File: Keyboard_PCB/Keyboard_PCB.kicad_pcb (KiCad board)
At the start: 4 copper layers, 107 parts, among them J1 I2C_LCD, J2 USB-C 16P, J3 LCD_MODULE, J4 FPC 30, J5 JTAG, Q1 S8050, SW1 EC11E15244G1, SW2 BTN, SW3 BTN, SW4 BTN, U1 STM32F412CGUx, U2 USBLC6-2SC6, U5 MCP73871, U6 MCP73871, U7 W25Q128JVS, Y1 25MHz, Y2 32.768 KHz

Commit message: Battery charger layout done
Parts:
- removed C24: 22u, Capacitor_SMD:C_0603_1608Metric
- removed C25: 100n, Capacitor_SMD:C_0603_1608Metric
- removed C26, C27, C33, C34: 4u7, Capacitor_SMD:C_0603_1608Metric
- removed C31, C32: 10u, Capacitor_SMD:C_0603_1608Metric
- removed JP2: BAT_BYP, Jumper:SolderJumper-2_P1.3mm_Open_TrianglePad1.0x1.5mm
- removed R16, R17, R18, R19: 470, Resistor_SMD:R_0603_1608Metric
- removed R20, R21: 10k, Resistor_SMD:R_0603_1608Metric
- removed TP1, TP2: TestPoint, TestPoint:TestPoint_Pad_D1.0mm
- added D11: PG, LED_SMD:LED_0603_1608Metric, F.Cu at (100.0, 206.6)
- added D4: BAT54C, Package_TO_SOT_SMD:SOT-23, F.Cu at (116.8, 197.0)
- C15: value 10u -> 22u
- C17: value 22u -> 10u
- C19: value 100n -> 22u
- C20, C21: value 10u -> 1u
- C22, C23: value 22u -> 1u
- D5: value PG -> BAT54C; footprint LED_SMD:LED_0603_1608Metric -> Package_TO_SOT_SMD:SOT-23
- L2, L3: value 1u5 -> 1u
- Q1: footprint Package_TO_SOT_THT:TO-92_Inline -> Package_TO_SOT_SMD:SOT-23
- R10, R13: value 180k -> 470
- R11, R9: value 1M -> 470
- R12, R8: value 1M -> 10k
- TH1, TH2: value Thermistor_NTC -> 10k
- U2: value USBLC6-2SC6 -> ISL91127IR; footprint Package_TO_SOT_SMD:SOT-23-6 -> Package_DFN_QFN:QFN-20-1EP_4x4mm_P0.5mm_EP2.7x2.7mm_ThermalVias
- U3: value ~ -> USBLC6-2SC6; footprint Marijn_KiCad:QFN_DSJ -> Package_TO_SOT_SMD:SOT-23-6
- U4: value ~ -> ISL91127IR; footprint Marijn_KiCad:QFN_DSJ -> Package_DFN_QFN:QFN-20-1EP_4x4mm_P0.5mm_EP2.7x2.7mm_ThermalVias
- U5, U6: value MCP73871 -> MCP73833; footprint Package_DFN_QFN:QFN-20-1EP_4x4mm_P0.5mm_EP2.5x2.5mm -> Package_DFN_QFN:DFN-10-1EP_3x3mm_P0.5mm_EP1.58x2.35mm
- moved U3 149.2 mm to (245.7, 156.6), turned to 0 degrees
- moved FL1 134.9 mm to (230.5, 168.4)
- moved Q1 65.7 mm to (273.9, 139.4)
- moved BT2 60.5 mm to (113.0, 202.2)
- moved U2 57.4 mm to (132.1, 195.1), turned to 0 degrees
- moved L3 56.7 mm to (137.5, 196.1)
- moved U6 56.7 mm to (107.4, 204.0), turned to 0 degrees
- moved D8 55.6 mm to (100.0, 199.9), turned to 180 degrees
- moved D10 55.6 mm to (100.0, 205.1), turned to 180 degrees
- moved D9 54.5 mm to (100.0, 203.5), turned to 180 degrees
- moved C20 51.0 mm to (105.9, 194.7), turned to 0 degrees
- moved C21 50.9 mm to (109.0, 194.7), turned to 180 degrees
- moved R11 47.8 mm to (103.1, 199.9), turned to 180 degrees
- moved TH2 46.7 mm to (110.4, 205.1), turned to -90 degrees
- moved U4 46.1 mm to (132.1, 201.3), turned to 0 degrees
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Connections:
- BT1 pad 1: Net-(BT1-+) -> /USB_PWR/APP_BAT
- BT2 pad 1: Net-(BT2-+) -> /USB_PWR/BKUP_BAT
- C14 pad 1: V_IN -> PVIN
- C15 pad 1: V_IN -> +3V3
- C17 pad 1: +3V3 -> PVIN
- C18 pad 1: +3V3 -> /VBAT
- C19 pad 1: Net-(U3-EN) -> /VBAT
- C20 pad 1: VIN -> +5V
- C21 pad 1: VIN -> /USB_PWR/APP_BAT
- C22 pad 1: /VBAT -> +5V
- C23 pad 1: /VBAT -> /USB_PWR/BKUP_BAT
- D5 pad 1: Net-(D5-K) -> /USB_PWR/BKUP_BAT
- Q1 pad 1: GND -> Net-(Q1-B)
- Q1 pad 2: Net-(Q1-B) -> GND
- R10 pad 1: Net-(U3-FB) -> Net-(U5-STAT2)
- R10 pad 2: GND -> Net-(D7-K)
- R11 pad 1: /VBAT -> Net-(U5-~{PG})
- R11 pad 2: Net-(U4-FB) -> Net-(D8-K)
- R12 pad 1: /VBAT -> GND
- R12 pad 2: /USB_PWR/PG1 -> /USB_PWR/BKUP_PROG
- R13 pad 1: Net-(U4-FB) -> Net-(U6-STAT1)
- R13 pad 2: GND -> Net-(D9-K)
- R14 pad 1: Net-(D5-K) -> Net-(U6-STAT2)
- R14 pad 2: /USB_PWR/APP_PG -> Net-(D10-K)
- R15 pad 1: Net-(D6-K) -> Net-(U6-~{PG})
- R15 pad 2: /USB_PWR/APP_STAT1 -> Net-(D11-K)
- R8 pad 1: +3V3 -> GND
- R8 pad 2: Net-(U3-FB) -> /USB_PWR/APP_PROG
- R9 pad 1: +3V3 -> Net-(U5-STAT1)
- R9 pad 2: /USB_PWR/PG0 -> Net-(D6-K)
- U1 pad 18: /APP_FC -> unconnected-(U1-PB0-Pad18)
- U1 pad 19: /BKUP_FC -> unconnected-(U1-PB1-Pad19)
- U2 pad 1: Net-(J2-D--PadA7) -> Net-(L2-Pad2)
- U2 pad 2: GND -> Net-(L2-Pad2)
- U2 pad 3: Net-(J2-D+-PadA6) -> GND
- U2 pad 4: Net-(FL1-Pad4) -> Net-(L2-Pad1)
- U2 pad 5: +5V -> Net-(L2-Pad1)
- U2 pad 6: Net-(FL1-Pad1) -> PVIN
- U3 pad 1: Net-(U3-EN) -> Net-(J2-D--PadA7)
- U3 pad 3: Net-(U3-FB) -> Net-(J2-D+-PadA6)
- U3 pad 4: +3V3 -> Net-(FL1-Pad4)
- U3 pad 5: +3V3 -> +5V
- U3 pad 6: Net-(L2-Pad2) -> Net-(FL1-Pad1)
- U4 pad 1: Net-(U4-EN) -> Net-(L3-Pad2)
- U4 pad 10: VIN -> PVIN
- U4 pad 11: VIN -> PVIN
- U4 pad 12: Net-(U4-EN) -> PVIN
- U4 pad 13: Net-(U4-EN) -> GND
- U4 pad 14: /USB_PWR/PG1 -> GND
- U4 pad 15: GND -> /VBAT
- U4 pad 2: GND -> Net-(L3-Pad2)
- U4 pad 3: Net-(U4-FB) -> GND
- U4 pad 4: /VBAT -> Net-(L3-Pad1)
- U4 pad 5: /VBAT -> Net-(L3-Pad1)
- U4 pad 6: Net-(L3-Pad2) -> PVIN
- U4 pad 7: Net-(L3-Pad2) -> PVIN
- U4 pad 8: Net-(L3-Pad1) -> PVIN
- U4 pad 9: Net-(L3-Pad1) -> PVIN
- U5 pad 1: V_IN -> +5V
- U5 pad 10: GND -> /USB_PWR/APP_BAT
- U5 pad 3: GND -> Net-(U5-STAT1)
- U5 pad 4: /APP_FC -> Net-(U5-STAT2)
- U5 pad 5: /USB_PWR/APP_THERM -> GND
- U5 pad 6: /USB_PWR/APP_PG -> /USB_PWR/APP_PROG
- U5 pad 7: /USB_PWR/APP_STAT2 -> Net-(U5-~{PG})
- U5 pad 8: /USB_PWR/APP_STAT1 -> /USB_PWR/APP_THERM
- U5 pad 9: +5V -> /USB_PWR/APP_BAT
- U6 pad 1: VIN -> +5V
- U6 pad 10: GND -> /USB_PWR/BKUP_BAT
- U6 pad 3: GND -> Net-(U6-STAT1)
- U6 pad 4: /BKUP_FC -> Net-(U6-STAT2)
- U6 pad 5: /USB_PWR/BKUP_THERM -> GND
- U6 pad 6: /USB_PWR/BKUP_PG -> /USB_PWR/BKUP_PROG
- U6 pad 7: /USB_PWR/BKUP_STAT2 -> Net-(U6-~{PG})
- U6 pad 8: /USB_PWR/BKUP_STAT1 -> /USB_PWR/BKUP_THERM
- U6 pad 9: +5V -> /USB_PWR/BKUP_BAT
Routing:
- net +5V: track 10.9 -> 27.3 mm, vias 4 -> 0
- net /USB_PWR/APP_STAT2: track 13.6 -> 0.00 mm, vias 2 -> 0
- net /USB_PWR/APP_PG: track 13.4 -> 0.00 mm, vias 2 -> 0
- net /USB_PWR/PG0: track 12.8 -> 0.00 mm, vias 2 -> 0
- net /USB_PWR/PG1: track 12.8 -> 0.00 mm, vias 2 -> 0
- net /USB_PWR/APP_STAT1: track 10.4 -> 0.00 mm, vias 2 -> 0
- net GND: track 13.7 -> 4.31 mm, vias 73 -> 0
- net Net-(U5-~{PG}): track 0.00 -> 8.08 mm, vias 0 -> 2
- net Net-(U6-~{PG}): track 0.00 -> 8.07 mm, vias 0 -> 2
- net Net-(U4-EN): track 7.45 -> 0.00 mm, vias 2 -> 0
- net Net-(U3-EN): track 7.45 -> 0.00 mm, vias 2 -> 0
- net Net-(U4-FB): track 3.13 -> 0.00 mm
- net Net-(U3-FB): track 3.13 -> 0.00 mm
- net Net-(U6-STAT2): track 0.00 -> 2.32 mm
- net Net-(U5-STAT2): track 0.00 -> 2.32 mm
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- added copper zone on F.Cu, net /USB_PWR/APP_BAT
- added copper zone on F.Cu, net /USB_PWR/APP_PROG
- added copper zone on F.Cu, net /USB_PWR/BKUP_BAT
- added copper zone on F.Cu, net /USB_PWR/BKUP_PROG
- removed copper zone on F.Cu, net +3V3
- removed copper zone on F.Cu, net +5V
- removed copper zone on F.Cu, net /VBAT
- removed copper zone on F.Cu, net GND
- removed copper zone on F.Cu, net Net-(BT1-+)
- removed copper zone on F.Cu, net Net-(L2-Pad1)
- removed copper zone on F.Cu, net Net-(L2-Pad2)
- removed copper zone on F.Cu, net Net-(L3-Pad1)
- removed copper zone on F.Cu, net Net-(L3-Pad2)
- removed copper zone on F.Cu, net VIN
- removed copper zone on F.Cu, net V_IN

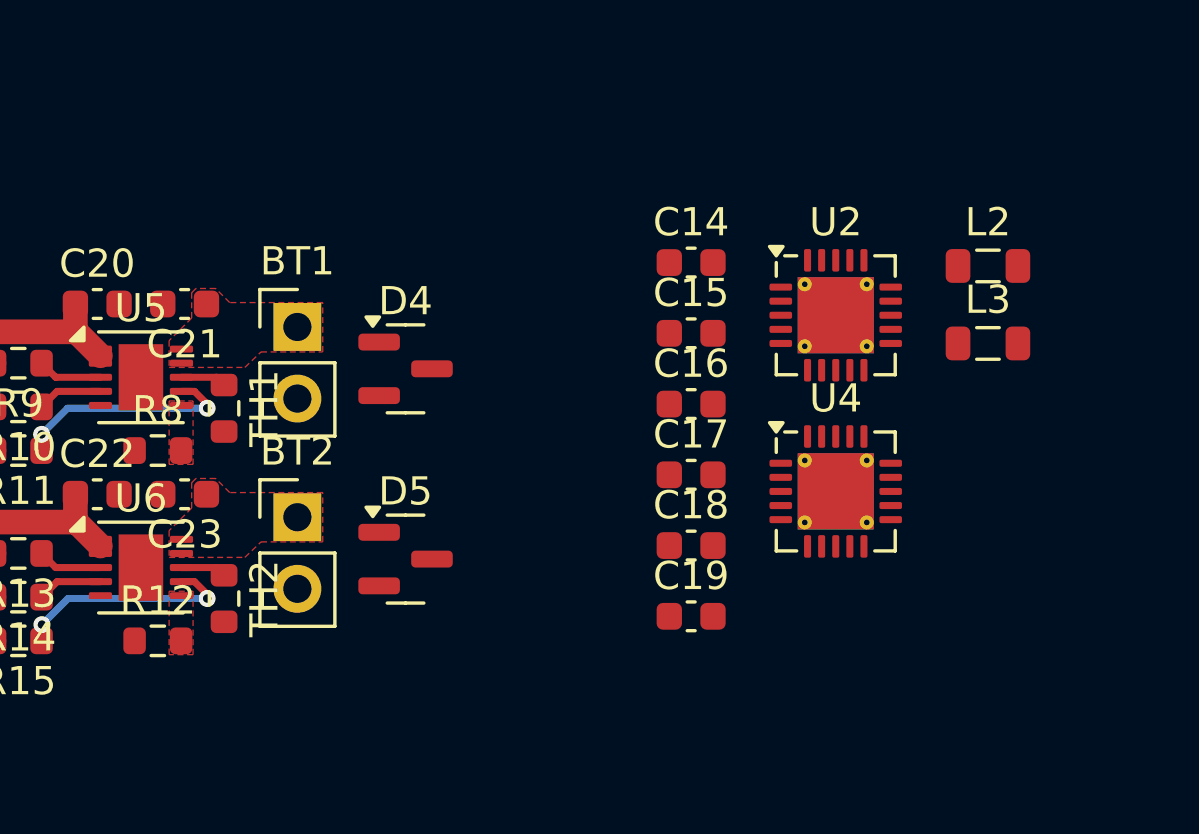
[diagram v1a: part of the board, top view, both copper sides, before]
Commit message: Buck layout progress
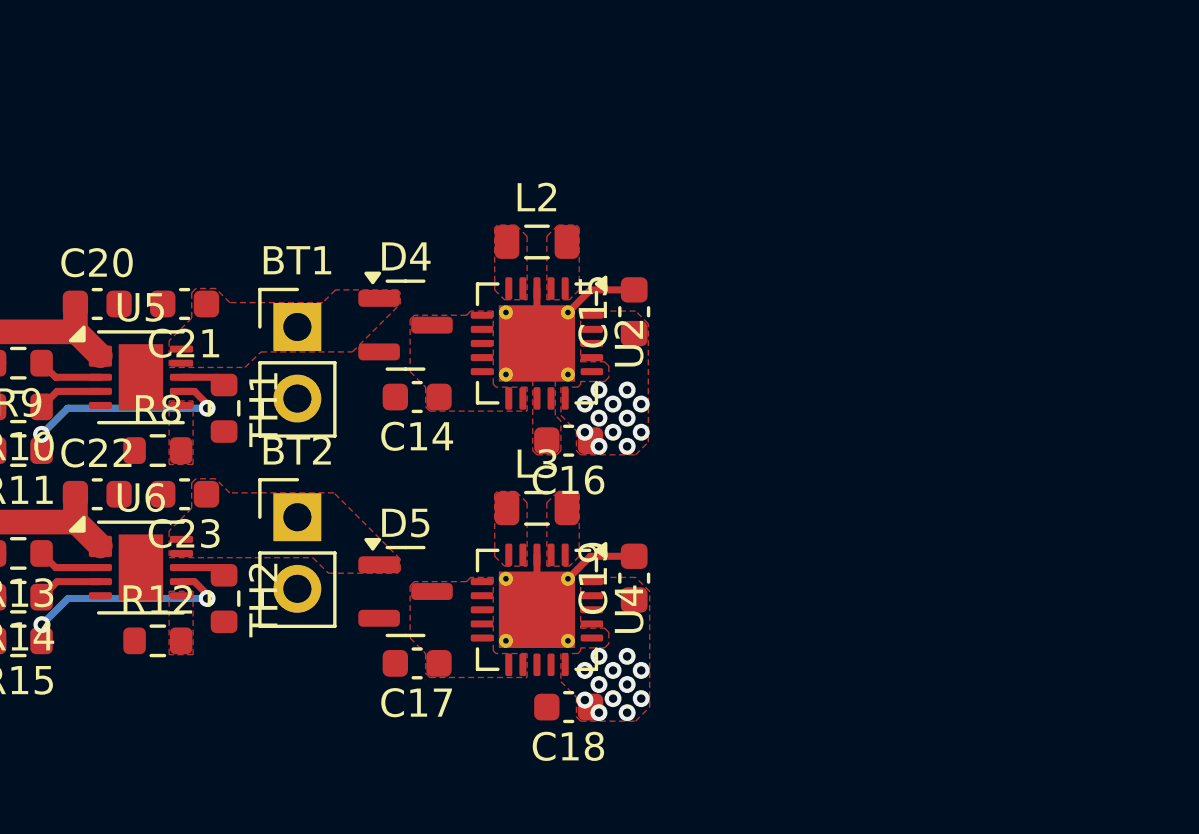
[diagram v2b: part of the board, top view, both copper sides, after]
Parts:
- moved L3 17.0 mm to (121.5, 201.9)
- moved L2 16.0 mm to (121.5, 192.5)
- moved C17 11.8 mm to (117.2, 207.4), turned to 180 degrees
- moved U4 11.4 mm to (121.5, 205.5), turned to -90 degrees
- moved C14 10.8 mm to (117.2, 198.0), turned to 180 degrees
- moved U2 10.6 mm to (121.5, 196.1), turned to -90 degrees
- moved C18 7.19 mm to (122.6, 209.0), turned to 180 degrees
- moved C16 4.54 mm to (122.6, 199.5), turned to 180 degrees
- moved C19 2.43 mm to (124.9, 204.4), turned to 90 degrees
- moved C15 2.16 mm to (124.9, 194.9), turned to 90 degrees
- moved D4 1.55 mm to (116.8, 195.4)
- moved D5 1.15 mm to (116.8, 204.9)
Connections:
- C14 pad 1: PVIN -> /USB_PWR/PVIN_APP
- C17 pad 1: PVIN -> /USB_PWR/PVIN_BKUP
- D4 pad 3: PVIN -> /USB_PWR/PVIN_APP
- D5 pad 3: PVIN -> /USB_PWR/PVIN_BKUP
- U2 pad 10: PVIN -> /USB_PWR/PVIN_APP
- U2 pad 11: PVIN -> /USB_PWR/PVIN_APP
- U2 pad 12: PVIN -> /USB_PWR/PVIN_APP
- U2 pad 6: PVIN -> /USB_PWR/PVIN_APP
- U2 pad 7: PVIN -> /USB_PWR/PVIN_APP
- U2 pad 8: PVIN -> /USB_PWR/PVIN_APP
- U2 pad 9: PVIN -> /USB_PWR/PVIN_APP
- U4 pad 10: PVIN -> /USB_PWR/PVIN_BKUP
- U4 pad 11: PVIN -> /USB_PWR/PVIN_BKUP
- U4 pad 12: PVIN -> /USB_PWR/PVIN_BKUP
- U4 pad 6: PVIN -> /USB_PWR/PVIN_BKUP
- U4 pad 7: PVIN -> /USB_PWR/PVIN_BKUP
- U4 pad 8: PVIN -> /USB_PWR/PVIN_BKUP
- U4 pad 9: PVIN -> /USB_PWR/PVIN_BKUP
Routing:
- net GND: track 4.31 -> 15.1 mm
- net /VBAT: vias 0 -> 12
- net +3V3: vias 0 -> 12
- added copper zone on F.Cu, net +3V3
- added copper zone on F.Cu, net /USB_PWR/PVIN_APP
- added copper zone on F.Cu, net /USB_PWR/PVIN_BKUP
- added copper zone on F.Cu, net /VBAT
- added copper zone on F.Cu, net GND
- added copper zone on F.Cu, net Net-(L2-Pad1)
- added copper zone on F.Cu, net Net-(L2-Pad2)
- added copper zone on F.Cu, net Net-(L3-Pad1)
- added copper zone on F.Cu, net Net-(L3-Pad2)

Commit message: Buck layout finished
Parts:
- added H1: MountingHole_Pad, MountingHole:MountingHole_2.2mm_M2_Pad_Via, F.Cu at (88.0, 192.1)
- added H2: MountingHole_Pad, MountingHole:MountingHole_2.2mm_M2_Pad_Via, F.Cu at (129.0, 192.1)
- U3: moved to B.Cu
- moved Q1 198.0 mm to (104.0, 241.0)
- moved U3 163.5 mm to (88.2, 200.6), turned to 180 degrees
- moved C10 138.7 mm to (84.7, 232.8)
- moved C11 138.7 mm to (84.7, 235.3)
- moved C12 138.7 mm to (84.7, 237.9)
- moved C13 138.7 mm to (84.7, 240.4)
- moved C28 138.7 mm to (84.7, 242.9)
- moved C29 138.7 mm to (84.7, 245.4)
- moved C30 138.7 mm to (84.7, 247.9)
- moved C35 138.7 mm to (84.7, 250.4)
- moved C4 138.7 mm to (80.7, 240.4)
- moved C7 138.7 mm to (80.7, 247.9)
- moved J1 138.7 mm to (108.4, 253.5)
- moved J3 138.7 mm to (97.0, 233.9)
- moved JP1 138.7 mm to (101.5, 267.2)
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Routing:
- net Net-(FL1-Pad4): track 0.00 -> 14.1 mm, vias 0 -> 1
- net +5V: track 27.3 -> 40.9 mm, vias 0 -> 11
- net Net-(FL1-Pad1): track 0.00 -> 9.50 mm, vias 0 -> 1
- net GND: track 15.1 -> 23.2 mm, vias 0 -> 46
- net Net-(J2-D--PadA7): track 3.92 -> 5.65 mm
- net Net-(J2-D+-PadA6): track 3.92 -> 5.65 mm
- net Net-(F1-Pad1): track 9.51 -> 8.02 mm
- net /USB_SENS: track 8.60 -> 9.94 mm
- added copper zone on B.Cu, net +5V
- added copper zone on F.Cu, net +5V
- added copper zone on B.Cu, net GND
- added copper zone on In1.Cu, net GND
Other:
- board outline added: 47 x 21.5 mm

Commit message: Power section finished
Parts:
- added JP2: WKUP_EXTI, Jumper:SolderJumper-2_P1.3mm_Open_TrianglePad1.0x1.5mm, F.Cu at (126.1, 239.9)
- added TP1: 5V, TestPoint:TestPoint_Pad_D2.0mm, F.Cu at (97.0, 198.3)
- added TP2: 3V3, TestPoint:TestPoint_Pad_D1.5mm, F.Cu at (125.3, 201.0)
- added TP3: Vbat, TestPoint:TestPoint_Pad_D1.5mm, F.Cu at (125.3, 206.6)
- J3: footprint Connector_PinHeader_2.54mm:PinHeader_1x08_P2.54mm_Vertical -> Connector_PinHeader_2.54mm:PinHeader_2x04_P2.54mm_Vertical
- SW2: footprint Button_Switch_SMD:SW_SPST_PTS810 -> Button_Switch_Keyboard:SW_Cherry_MX_1.00u_PCB
- moved H2 44.4 mm to (88.0, 209.1)
- moved SW2 39.5 mm to (142.0, 248.9)
- moved J3 17.9 mm to (95.3, 251.7)
- moved FL1 11.4 mm to (92.2, 207.8), turned to 0 degrees
- moved SW1 10.8 mm to (121.3, 263.8), turned to 90 degrees
- moved U1 1.47 mm to (112.9, 238.9)
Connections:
- U1 pad 18: unconnected-(U1-PB0-Pad18) -> Net-(JP2-B)
- U1 pad 19: unconnected-(U1-PB1-Pad19) -> /ENC_SW
- U1 pad 20: /ENC_SW -> unconnected-(U1-PB2-Pad20)
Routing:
- net Net-(FL1-Pad4): track 14.1 -> 9.13 mm
- net +3V3: track 0.00 -> 3.03 mm
- net Net-(FL1-Pad1): track 9.50 -> 11.8 mm
- net GND: vias 46 -> 90
- net /VBAT: vias 12 -> 0
- added copper zone on In2.Cu, net +3V3
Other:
- board size 47 x 21.5 mm -> 41.8 x 21.5 mm

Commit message: Layout V1
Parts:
- added H3: MountingHole_Pad, MountingHole:MountingHole_2.2mm_M2_Pad_Via, F.Cu at (88.0, 248.6)
- added H4: MountingHole_Pad, MountingHole:MountingHole_2.2mm_M2_Pad_Via, F.Cu at (124.0, 248.6)
- C11, C12, Q1, R26, R27, R28: moved to B.Cu
- moved JP1 60.7 mm to (124.8, 211.2)
- moved D2 58.7 mm to (125.6, 217.1), turned to 90 degrees
- moved D1 55.7 mm to (124.0, 217.1), turned to 90 degrees
- moved SW4 54.6 mm to (119.3, 211.1)
- moved R25 53.6 mm to (125.6, 214.0), turned to -90 degrees
- moved R24 50.7 mm to (124.0, 214.0), turned to -90 degrees
- moved L1 50.2 mm to (112.7, 216.8), turned to -135 degrees
- moved Y1 48.9 mm to (112.2, 221.1), turned to 45 degrees
- moved SW3 48.4 mm to (113.5, 211.1)
- moved R22 48.1 mm to (119.5, 208.4), turned to 180 degrees
- moved C8 46.8 mm to (114.2, 217.8), turned to 45 degrees
- moved R23 46.5 mm to (113.3, 208.4)
- moved C9 45.7 mm to (124.1, 238.7), turned to 180 degrees
- moved SW2 45.5 mm to (98.7, 234.9)
- moved C2 43.7 mm to (124.1, 240.2), turned to 180 degrees
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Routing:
- net GND: track 23.2 -> 86.2 mm, vias 90 -> 224
- net /ENC_SW: track 0.00 -> 52.3 mm, vias 0 -> 3
- net /ENC_A: track 0.00 -> 44.6 mm, vias 0 -> 2
- net /ENC_B: track 0.00 -> 40.4 mm, vias 0 -> 2
- net /USB_SENS: track 9.94 -> 47.4 mm, vias 2 -> 6
- net /SWDIO: track 0.00 -> 36.3 mm, vias 0 -> 3
- net /LCD_NRST: track 0.00 -> 35.9 mm, vias 0 -> 3
- net /SWCLK: track 0.00 -> 34.5 mm, vias 0 -> 1
- net /LCD_DC: track 0.00 -> 33.9 mm, vias 0 -> 3
- net /LCD_CLK: track 0.00 -> 31.9 mm, vias 0 -> 2
- net +3V3: track 3.03 -> 32.1 mm, vias 12 -> 32
- net /LCD_NCS: track 0.00 -> 28.7 mm, vias 0 -> 3
- net /LCD_MOSI: track 0.00 -> 28.0 mm, vias 0 -> 3
- net /VBAT: track 0.00 -> 27.2 mm, vias 0 -> 2
- net Net-(JP2-B): track 0.00 -> 26.5 mm, vias 0 -> 2
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- added copper zone on F.Cu, net /BOOT0
- added copper zone on F.Cu, net /NRST
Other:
- board size 41.8 x 21.5 mm -> 42 x 62.5 mm

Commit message: Layout V1.1 + gerbers
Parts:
- added JP3: VBAT_BYP, Jumper:SolderJumper-2_P1.3mm_Open_TrianglePad1.0x1.5mm, B.Cu at (125.3, 208.5)
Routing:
- net /USB_SENS: track 47.4 -> 50.1 mm
- net /VBAT: track 27.2 -> 28.7 mm
- net +3V3: track 32.1 -> 32.6 mm, vias 32 -> 33
- net GND: vias 224 -> 261
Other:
- board text added: "BT1"
- board text added: "BT2"
- board text added: "FPC_30"
- board text added: "I2C_LCD"
- board text added: "J1"
- board text added: "J3"
- board text added: "J5"
- board text added: "JTAG"
- board text added: "KB PCB V0"
- board text added: "PWR"
- board text added: "ROT/BTN"
- board text added: "SPI_LCD"
- board text added: "STAT"
- board text added: "SW1"
- board text added: "SW2"
- board text added: "VBAT_BYP"
- board text added: "WKUP/BTN"
- board text added: "WKUP_EXTI"
